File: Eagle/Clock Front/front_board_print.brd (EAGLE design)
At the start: 14 parts

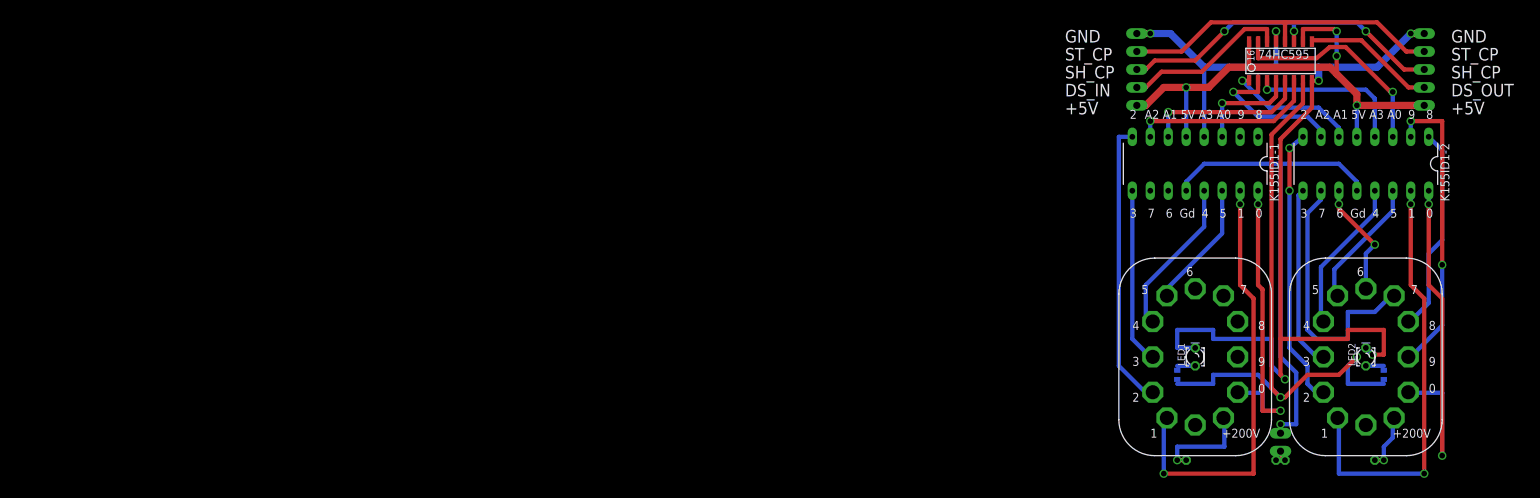
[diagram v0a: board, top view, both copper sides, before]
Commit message: Обновление печатной платы для цоколей. Подготовка к печати
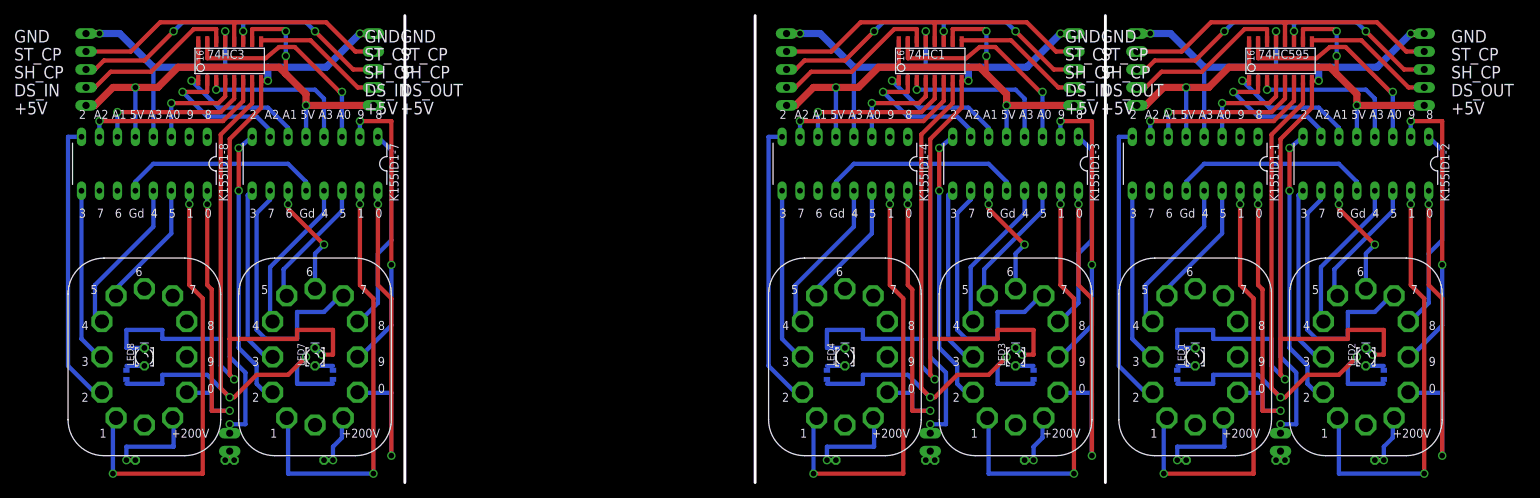
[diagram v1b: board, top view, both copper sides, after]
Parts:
- added 200VCONNECTOR1, 200VCONNECTOR3: (no value), pinhead:1X02
- added 74HC1, 74HC3: (no value), texas:SO-16
- added E$13, E$14, E$5, E$6: (no value), _ArSoron:IN-12
- added E$15, E$16, E$7, E$8: (no value), rcl:0309/12
- added IN1, IN3, OUT1, OUT3: (no value), pinhead:1X05
- added K155ID1-3, K155ID1-4, K155ID1-7, K155ID1-8: (no value), _ArSoron:K155ID1
- added LED3, LED4, LED7, LED8: (no value), eagle-ltspice:LED_LD260
- added R3, R4, R7, R8: (no value), eagle-ltspice:R0402
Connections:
- new net +200V1: 200VCONNECTOR1.1, E$7.1, E$8.2
- new net +200V3: 200VCONNECTOR3.1, E$15.1, E$16.2
- new net +5V1: IN1.1, K155ID1-3.5, K155ID1-4.5, OUT1.1
- new net +5V3: IN3.1, K155ID1-7.5, K155ID1-8.5, OUT3.1
- new net DATA_IN1: IN1.2
- new net DATA_IN3: IN3.2
- new net DATA_OUT1: OUT1.2
- new net DATA_OUT3: OUT3.2
- new net GND_HIGH1: K155ID1-3.12, K155ID1-4.12
- new net GND_HIGH3: K155ID1-7.12, K155ID1-8.12
- new net GND_LOW1: IN1.5, K155ID1-4.4, LED3.K, LED4.K
- new net GND_LOW3: IN3.5, K155ID1-8.4, LED7.K, LED8.K
- new net S$100: K155ID1-8.3
- new net S$101: K155ID1-7.4
- new net S$102: K155ID1-7.7
- new net S$103: K155ID1-7.6
- new net S$104: K155ID1-7.3
- new net S$27: K155ID1-3.1
- new net S$28: K155ID1-3.2
- new net S$29: K155ID1-3.16
- new net S$30: K155ID1-3.9
- new net S$31: K155ID1-3.8
- new net S$32: K155ID1-3.13
- new net S$33: K155ID1-3.14
- new net S$34: K155ID1-3.10
- new net S$35: K155ID1-3.11
- new net S$37: K155ID1-3.15
- new net S$38: LED3.A
- new net S$39: K155ID1-4.16
- new net S$40: K155ID1-4.9
- new net S$41: K155ID1-4.8
- new net S$42: K155ID1-4.13
- new net S$43: K155ID1-4.14
- new net S$44: K155ID1-4.15
- new net S$45: LED4.A
- new net S$46: K155ID1-4.7
- new net S$47: K155ID1-4.6
- new net S$48: K155ID1-4.3
- new net S$49: K155ID1-3.4
- new net S$50: K155ID1-3.7
- new net S$51: K155ID1-3.6
- new net S$52: K155ID1-3.3
- new net S$79: K155ID1-7.1
- new net S$80: K155ID1-7.2
- new net S$81: K155ID1-7.16
- new net S$82: K155ID1-7.9
- new net S$83: K155ID1-7.8
- new net S$84: K155ID1-7.13
- new net S$85: K155ID1-7.14
- new net S$86: K155ID1-7.10
- new net S$87: K155ID1-7.11
- new net S$89: K155ID1-7.15
- new net S$90: LED7.A
- new net S$91: K155ID1-8.16
- new net S$92: K155ID1-8.9
- new net S$93: K155ID1-8.8
- new net S$94: K155ID1-8.13
- new net S$95: K155ID1-8.14
- new net S$96: K155ID1-8.15
- new net S$97: LED8.A
- new net S$98: K155ID1-8.7
- new net S$99: K155ID1-8.6
- new net SH_CP1: IN1.3, OUT1.3
- new net SH_CP3: IN3.3, OUT3.3
- new net ST_CP1: IN1.4, OUT1.4
- new net ST_CP3: IN3.4, OUT3.4
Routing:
- net GND_LOW1: track 0.00 -> 157.1 mm, vias 0 -> 6
- net GND_LOW3: track 0.00 -> 157.1 mm, vias 0 -> 6
- net LED+3: track 0.00 -> 86.6 mm, vias 0 -> 2
- net LED+1: track 0.00 -> 86.6 mm, vias 0 -> 2
- net +5V1: track 0.00 -> 74.4 mm, vias 0 -> 4
- net +5V3: track 0.00 -> 74.4 mm, vias 0 -> 4
- net GND_HIGH3: track 0.00 -> 70.0 mm, vias 0 -> 1
- net GND_HIGH1: track 0.00 -> 70.0 mm, vias 0 -> 1
- net S$44: track 0.00 -> 61.1 mm, vias 0 -> 2
- net S$96: track 0.00 -> 61.1 mm, vias 0 -> 2
- net S$81: track 0.00 -> 51.6 mm, vias 0 -> 2
- net S$29: track 0.00 -> 51.6 mm, vias 0 -> 2
- net SH_CP3: track 0.00 -> 49.3 mm, vias 0 -> 3
- net SH_CP1: track 0.00 -> 49.3 mm, vias 0 -> 3
- net ST_CP1: track 0.00 -> 47.2 mm
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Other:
- board outline added: 99.1 x 66 mm
